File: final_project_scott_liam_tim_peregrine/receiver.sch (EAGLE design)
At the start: 22 parts

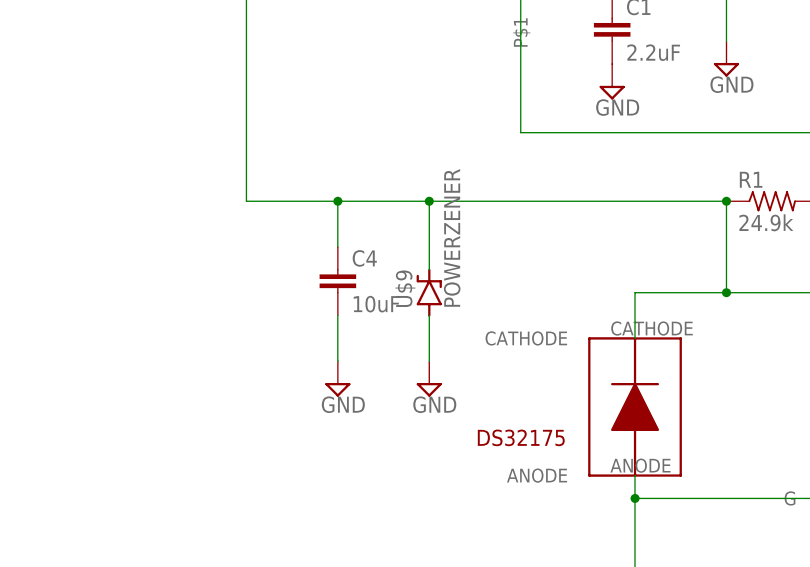
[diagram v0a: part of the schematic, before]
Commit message: added receiver board
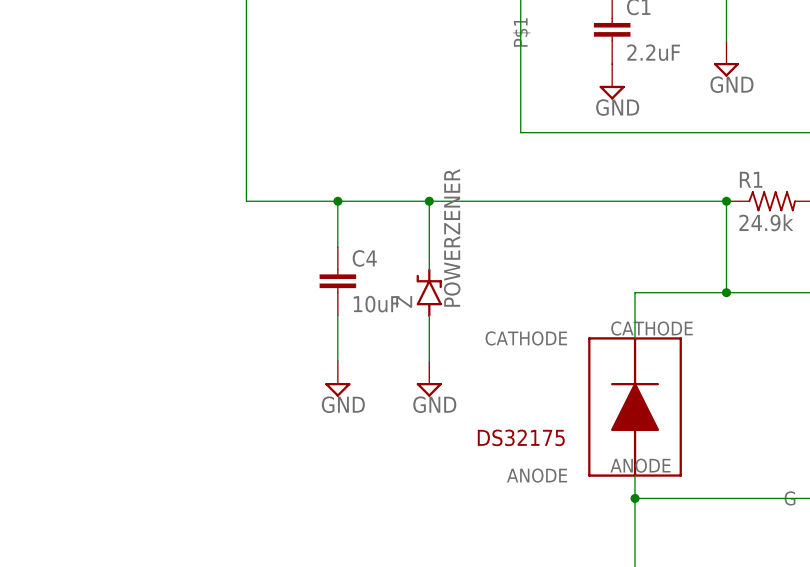
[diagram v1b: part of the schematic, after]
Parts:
- renumbered U$7 to PS, U$8 to PS2, U$9 to Z
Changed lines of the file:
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@@
 <?xml version="1.0" encoding="utf-8"?>
 <!DOCTYPE eagle SYSTEM "eagle.dtd">
-<eagle version="7.5.0">
+<eagle version="7.4.0">
 <drawing>
 <settings>
@@
 <grid distance="0.1" unitdist="inch" unit="inch" style="lines" multiple="1" display="no" altdistance="0.01" altunitdist="inch" altunit="inch"/>
 <layers>
-<layer number="1" name="Top" color="4" fill="1" visible="no" active="no"/>
-<layer number="16" name="Bottom" color="1" fill="1" visible="no" active="no"/>
-<layer number="17" name="Pads" color="2" fill="1" visible="no" active="no"/>
-<layer number="18" name="Vias" color="2" fill="1" visible="no" active="no"/>
-<layer number="19" name="Unrouted" color="6" fill="1" visible="no" active="no"/>
-<layer number="20" name="Dimension" color="15" fill="1" visible="no" active="no"/>
-<layer number="21" name="tPlace" color="7" fill="1" visible="no" active="no"/>
-<layer number="22" name="bPlace" color="7" fill="1" visible="no" active="no"/>
-<layer number="23" name="tOrigins" color="15" fill="1" visible="no" active="no"/>
-<layer number="24" name="bOrigins" color="15" fill="1" visible="no" active="no"/>
-<layer number="25" name="tNames" color="7" fill="1" visible="no" active="no"/>
-<layer number="26" name="bNames" color="7" fill="1" visible="no" active="no"/>
-<layer number="27" name="tValues" color="7" fill="1" visible="no" active="no"/>
-<layer number="28" name="bValues" color="7" fill="1" visible="no" active="no"/>
+<layer number="1" name="Top" color="4" fill="1" visible="yes" active="no"/>
+<layer number="16" name="Bottom" color="1" fill="1" visible="yes" active="no"/>
+<layer number="17" name="Pads" color="2" fill="1" visible="yes" active="no"/>
+<layer number="18" name="Vias" color="2" fill="1" visible="yes" active="no"/>
+<layer number="19" name="Unrouted" color="6" fill="1" visible="yes" active="no"/>
+<layer number="20" name="Dimension" color="15" fill="1" visible="yes" active="no"/>
+<layer number="21" name="tPlace" color="7" fill="1" visible="yes" active="no"/>
+<layer number="22" name="bPlace" color="7" fill="1" visible="yes" active="no"/>
+<layer number="23" name="tOrigins" color="15" fill="1" visible="yes" active="no"/>
+<layer number="24" name="bOrigins" color="15" fill="1" visible="yes" active="no"/>
+<layer number="25" name="tNames" color="7" fill="1" visible="yes" active="no"/>
+<layer number="26" name="bNames" color="7" fill="1" visible="yes" active="no"/>
+<layer number="27" name="tValues" color="7" fill="1" visible="yes" active="no"/>
+<layer number="28" name="bValues" color="7" fill="1" visible="yes" active="no"/>
 <layer number="29" name="tStop" color="7" fill="3" visible="no" active="no"/>
 <layer number="30" name="bStop" color="7" fill="6" visible="no" active="no"/>
@@
 <layer number="35" name="tGlue" color="7" fill="4" visible="no" active="no"/>
 <layer number="36" name="bGlue" color="7" fill="5" visible="no" active="no"/>
-<layer number="37" name="tTest" color="7" fill="1" visible="no" active="no"/>
-<layer number="38" name="bTest" color="7" fill="1" visible="no" active="no"/>
+<layer number="37" name="tTest" color="7" fill="1" visible="yes" active="no"/>
+<layer number="38" name="bTest" color="7" fill="1" visible="yes" active="no"/>
 <layer number="39" name="tKeepout" color="4" fill="11" visible="no" active="no"/>
 <layer number="40" name="bKeepout" color="1" fill="11" visible="no" active="no"/>
@@
 <layer number="44" name="Drills" color="7" fill="1" visible="no" active="no"/>
 <layer number="45" name="Holes" color="7" fill="1" visible="no" active="no"/>
-<layer number="46" name="Milling" color="3" fill="1" visible="no" active="no"/>
-<layer number="47" name="Measures" color="7" fill="1" visible="no" active="no"/>
-<layer number="48" name="Document" color="7" fill="1" visible="no" active="no"/>
-<layer number="49" name="Reference" color="7" fill="1" visible="no" active="no"/>
-<layer number="51" name="tDocu" color="7" fill="1" visible="no" active="no"/>
-<layer number="52" name="bDocu" color="7" fill="1" visible="no" active="no"/>
+<layer number="46" name="Milling" color="3" fill="1" visible="yes" active="no"/>
+<layer number="47" name="Measures" color="7" fill="1" visible="yes" active="no"/>
+<layer number="48" name="Document" color="7" fill="1" visible="yes" active="no"/>
+<layer number="49" name="Reference" color="7" fill="1" visible="yes" active="no"/>
+<layer number="51" name="tDocu" color="7" fill="1" visible="yes" active="no"/>
+<layer number="52" name="bDocu" color="7" fill="1" visible="yes" active="no"/>
 <layer number="90" name="Modules" color="5" fill="1" visible="yes" active="yes"/>
 <layer number="91" name="Nets" color="2" fill="1" visible="yes" active="yes"/>
@@
 <part name="C1" library="resistor" deviceset="C-EU" device="C0805K" value="2.2uF"/>
 <part name="C2" library="resistor" deviceset="C-EU" device="C0805K" value="10nF"/>
-<part name="U$3" library="foe-scale" deviceset="15UH-INDUCTOR" device=""/>
 <part name="R1" library="resistor" deviceset="R-US_" device="R0805" value="24.9k"/>
 <part name="U$4" library="foe-scale" deviceset="BAS521" device=""/>
@@
 <part name="SUPPLY6" library="supply2" deviceset="GND" device=""/>
 <part name="C5" library="resistor" deviceset="C-EU" device="C0805K" value="33nF"/>
-<part name="U$7" library="foe-scale" deviceset="SCHTKYPOWER" device=""/>
-<part name="U$8" library="foe-scale" deviceset="SCHTKYPOWER" device=""/>
-<part name="U$9" library="foe-scale" deviceset="POWERZENER" device=""/>
+<part name="PS" library="foe-scale" deviceset="SCHTKYPOWER" device=""/>
+<part name="PS2" library="foe-scale" deviceset="SCHTKYPOWER" device=""/>
+<part name="Z" library="foe-scale" deviceset="POWERZENER" device=""/>
 <part name="SUPPLY7" library="supply2" deviceset="GND" device=""/>
 <part name="R3" library="resistor" deviceset="R-US_" device="R0805" value="3.01k"/>
@@
 <part name="R4" library="resistor" deviceset="R-US_" device="R0805" value="18"/>
 <part name="SUPPLY10" library="supply2" deviceset="GND" device=""/>
+<part name="U$3" library="foe-scale" deviceset="15UH-INDUCTOR" device=""/>
 </parts>
 <sheets>
@@
 <instance part="C1" gate="G$1" x="33.02" y="33.02"/>
 <instance part="C2" gate="G$1" x="22.86" y="68.58"/>
-<instance part="U$3" gate="G$1" x="22.86" y="38.1" rot="R90"/>
 <instance part="R1" gate="G$1" x="50.8" y="12.7"/>
 <instance part="U$4" gate="G$1" x="35.56" y="-10.16" rot="R180"/>
@@
 <instance part="SUPPLY6" gate="GND1" x="2.54" y="-7.62"/>
 <instance part="C5" gate="G$1" x="-35.56" y="83.82" rot="R90"/>
-<instance part="U$7" gate="G$1" x="-22.86" y="83.82" rot="R270"/>
-<instance part="U$8" gate="G$1" x="-30.48" y="78.74"/>
-<instance part="U$9" gate="G$1" x="12.7" y="2.54" rot="R90"/>
+<instance part="PS" gate="G$1" x="-22.86" y="83.82" rot="R270"/>
+<instance part="PS2" gate="G$1" x="-30.48" y="78.74"/>
+<instance part="Z" gate="G$1" x="12.7" y="2.54" rot="R90"/>
 <instance part="SUPPLY7" gate="GND1" x="-30.48" y="68.58"/>
 <instance part="R3" gate="G$1" x="73.66" y="101.6" rot="R90"/>
@@
 <instance part="R4" gate="G$1" x="99.06" y="-30.48" rot="R90"/>
 <instance part="SUPPLY10" gate="GND1" x="99.06" y="-45.72"/>
+<instance part="U$3" gate="G$1" x="22.86" y="38.1" rot="R90"/>
 </instances>
 <busses>
@@
 <pinref part="SUPPLY5" gate="GND1" pin="GND"/>
 <wire x1="12.7" y1="-5.08" x2="12.7" y2="0" width="0.1524" layer="91"/>
-<pinref part="U$9" gate="G$1" pin="A"/>
+<pinref part="Z" gate="G$1" pin="A"/>
 </segment>
 <segment>
@@
 </segment>
 <segment>
-<pinref part="U$8" gate="G$1" pin="A"/>
+<pinref part="PS2" gate="G$1" pin="A"/>
 <pinref part="SUPPLY7" gate="GND1" pin="GND"/>
 </segment>
@@
 <wire x1="38.1" y1="58.42" x2="17.78" y2="58.42" width="0.1524" layer="91"/>
 <junction x="-7.62" y="58.42"/>
-<pinref part="U$7" gate="G$1" pin="C"/>
+<pinref part="PS" gate="G$1" pin="C"/>
 <wire x1="17.78" y1="58.42" x2="-7.62" y2="58.42" width="0.1524" layer="91"/>
 <wire x1="-17.78" y1="83.82" x2="-7.62" y2="83.82" width="0.1524" layer="91"/>
-<pinref part="U$9" gate="G$1" pin="C"/>
+<pinref part="Z" gate="G$1" pin="C"/>
 <pinref part="U$1" gate="G$1" pin="RUN"/>
 <wire x1="50.8" y1="81.28" x2="50.8" y2="86.36" width="0.1524" layer="91"/>
@@
 <pinref part="U$1" gate="G$1" pin="SW"/>
 <wire x1="22.86" y1="53.34" x2="38.1" y2="53.34" width="0.1524" layer="91"/>
-<pinref part="U$3" gate="G$1" pin="P$2"/>
 <wire x1="22.86" y1="53.34" x2="22.86" y2="48.26" width="0.1524" layer="91"/>
 <junction x="22.86" y="53.34"/>
+<pinref part="U$3" gate="G$1" pin="P$2"/>
 </segment>
 </net>
 <net name="N$2" class="0">
 <segment>
-<pinref part="U$3" gate="G$1" pin="P$1"/>
 <wire x1="22.86" y1="35.56" x2="22.86" y2="20.32" width="0.1524" layer="91"/>
 <pinref part="U$1" gate="G$1" pin="CHGSNS"/>
 <wire x1="22.86" y1="20.32" x2="66.04" y2="20.32" width="0.1524" layer="91"/>
 <wire x1="66.04" y1="20.32" x2="66.04" y2="40.64" width="0.1524" layer="91"/>
+<pinref part="U$3" gate="G$1" pin="P$1"/>
 </segment>
 </net>
@@
 <segment>
 <pinref part="C5" gate="G$1" pin="2"/>
-<pinref part="U$8" gate="G$1" pin="C"/>
-<pinref part="U$7" gate="G$1" pin="A"/>
+<pinref part="PS2" gate="G$1" pin="C"/>
+<pinref part="PS" gate="G$1" pin="A"/>
 <junction x="-30.48" y="83.82"/>
 </segment>
